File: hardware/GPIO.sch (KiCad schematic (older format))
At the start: 19 parts, among them J10 USB_B, J8 Conn_02x10_Odd_Even, J9 Conn_01x06_Male, SW1 SW_Push, U3 PIC18F4550-IP, U4 74LS06, U5 74LS06

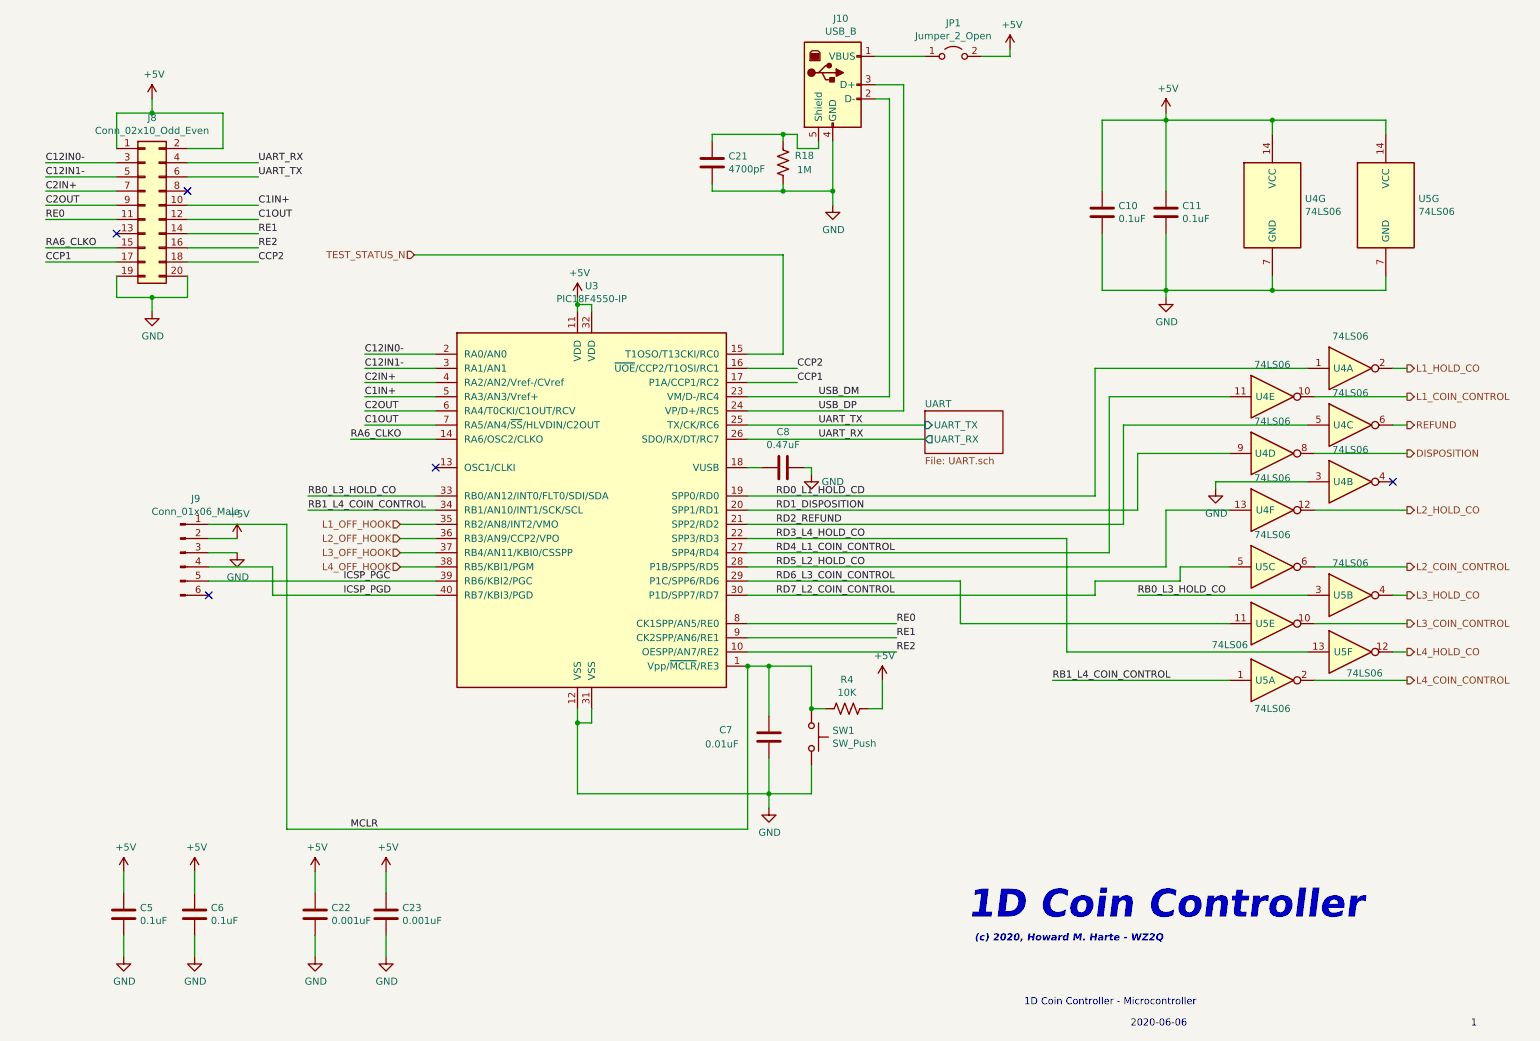
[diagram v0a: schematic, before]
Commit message: Issue 2 schmatic and Layout
Added polarity reversal detection to monitor answer supervision.
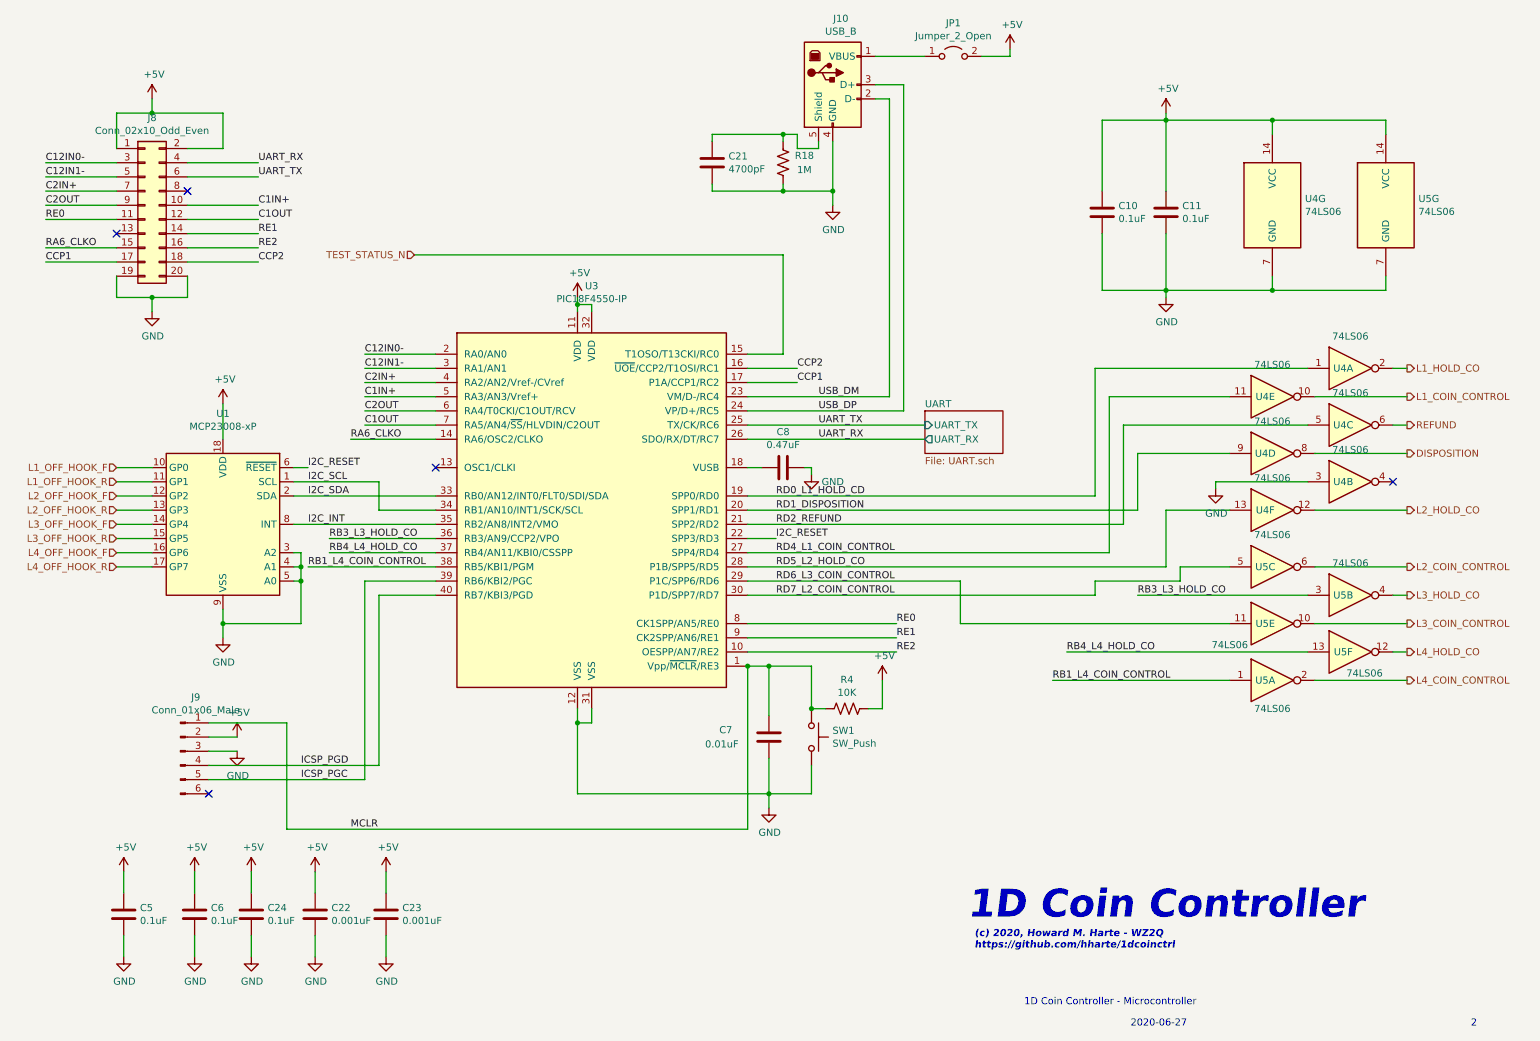
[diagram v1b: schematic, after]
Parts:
- added C24: 0.1uF, Capacitor_THT:C_Disc_D3.0mm_W2.0mm_P2.50mm, symbol Device:C
- added U1: MCP23008-xP, Package_DIP:DIP-18_W7.62mm, symbol Interface_Expansion:MCP23008-xP
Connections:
- net L4_OFF_HOOK is gone; now on net RB1_L4_COIN_CONTROL: U3.38 (RB5/KBI1/PGM)
- net +5V: now also C24.1, U1.18 (VDD)
- net GND: now also C24.2, U1.3 (A2), U1.4 (A1), U1.5 (A0), U1.9 (VSS)
- net RB1_L4_COIN_CONTROL: no longer U3.34 (RB1/AN10/INT1/SCK/SCL)
- net L1_OFF_HOOK renamed I2C_INT
- net I2C_INT: now also U1.8 (INT)
- net L2_OFF_HOOK renamed RB3_L3_HOLD_CO
- net RB3_L3_HOLD_CO: now also U5.3
- net L3_OFF_HOOK renamed RB4_L4_HOLD_CO
- net RB4_L4_HOLD_CO: now also U5.13
- net RB0_L3_HOLD_CO renamed I2C_SDA
- net I2C_SDA: now also U1.2 (SDA); no longer U5.3
- net RD3_L4_HOLD_CO renamed I2C_RESET
- net I2C_RESET: now also U1.6 (~RESET); no longer U5.13
- new net I2C_SCL: U1.1 (SCL), U3.34 (RB1/AN10/INT1/SCK/SCL)
- new net L1_OFF_HOOK_F: U1.10 (GP0)
- new net L1_OFF_HOOK_R: U1.11 (GP1)
- new net L2_OFF_HOOK_F: U1.12 (GP2)
- new net L2_OFF_HOOK_R: U1.13 (GP3)
- new net L3_OFF_HOOK_F: U1.14 (GP4)
- new net L3_OFF_HOOK_R: U1.15 (GP5)
- new net L4_OFF_HOOK_F: U1.16 (GP6)
- new net L4_OFF_HOOK_R: U1.17 (GP7)
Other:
- note added: "(c) 2020, Howard M. Harte - WZ2Q\nhttps://github.com/hharte/1dcoinctrl"
- note added: "2"
- note added: "2020-06-27"
- note removed: "(c) 2020, Howard M. Harte - WZ2Q"
- note removed: "1"
- note removed: "2020-06-06"
